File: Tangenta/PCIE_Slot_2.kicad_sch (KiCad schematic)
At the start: 12 parts, among them J19 1-2199230-5

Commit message: Removing component association with previous project (local) libraries.
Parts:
- C112, C113: footprint CholaFootprintsPrjLib:CAP_TANTAL_A -> CAP_TANTAL_A:CAP_TANTAL_A; symbol CholaSymbolsPrjLib:CA45-A-6_3V-47UF-K -> CA45-A-6_3V-47UF-K:CA45-A-6_3V-47UF-K
- H16, H17, H18: symbol CholaSymbolsPrjLib:MountingHole -> MountingHole:MountingHole
- J19: footprint CholaFootprintsPrjLib:M2_Slot -> M2_Slot:M2_Slot; symbol CholaSymbolsPrjLib:1-2199230-5 -> 1-2199230-5:1-2199230-5
- R83, R84, R85, R86, R87: symbol CholaSymbolsPrjLib:R_Small_US -> R_Small_US:R_Small_US
- TP2: symbol CholaSymbolsPrjLib:TestPoint_Small -> TestPoint_Small:TestPoint_Small
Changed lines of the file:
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@@
 	)
 	(symbol
-		(lib_id "CholaSymbolsPrjLib:MountingHole")
+		(lib_id "MountingHole:MountingHole")
 		(at 163.195 175.26 0)
 		(unit 1)
@@
 	)
 	(symbol
-		(lib_id "CholaSymbolsPrjLib:MountingHole")
+		(lib_id "MountingHole:MountingHole")
 		(at 163.195 185.42 0)
 		(unit 1)
@@
 	)
 	(symbol
-		(lib_id "CholaSymbolsPrjLib:R_Small_US")
+		(lib_id "R_Small_US:R_Small_US")
 		(at 161.29 48.26 270)
 		(unit 1)
@@
 	)
 	(symbol
-		(lib_id "CholaSymbolsPrjLib:1-2199230-5")
+		(lib_id "1-2199230-5:1-2199230-5")
 		(at 135.89 33.02 90)
 		(mirror x)
@@
 			)
 		)
-		(property "Footprint" "CholaFootprintsPrjLib:M2_Slot"
+		(property "Footprint" "M2_Slot:M2_Slot"
 			(at 225.73 128.27 0)
 			(effects
@@
 	(symbol
 		(lib_name "CA45-A-6_3V-47UF-K_1")
-		(lib_id "CholaSymbolsPrjLib:CA45-A-6_3V-47UF-K")
+		(lib_id "CA45-A-6_3V-47UF-K:CA45-A-6_3V-47UF-K")
 		(at 140.97 148.59 270)
 		(mirror x)
@@
 			)
 		)
-		(property "Footprint" "CholaFootprintsPrjLib:CAP_TANTAL_A"
+		(property "Footprint" "CAP_TANTAL_A:CAP_TANTAL_A"
 			(at 129.286 145.542 0)
 			(effects
@@
 	)
 	(symbol
-		(lib_id "CholaSymbolsPrjLib:MountingHole")
+		(lib_id "MountingHole:MountingHole")
 		(at 163.195 180.34 0)
 		(unit 1)
@@
 	)
 	(symbol
-		(lib_id "CholaSymbolsPrjLib:R_Small_US")
+		(lib_id "R_Small_US:R_Small_US")
 		(at 161.29 45.72 270)
 		(unit 1)
@@
 	)
 	(symbol
-		(lib_id "CholaSymbolsPrjLib:R_Small_US")
+		(lib_id "R_Small_US:R_Small_US")
 		(at 163.83 91.44 270)
 		(unit 1)
@@
 	)
 	(symbol
-		(lib_id "CholaSymbolsPrjLib:CA45-A-6_3V-47UF-K")
+		(lib_id "CA45-A-6_3V-47UF-K:CA45-A-6_3V-47UF-K")
 		(at 130.175 148.59 270)
 		(mirror x)
@@
 			)
 		)
-		(property "Footprint" "CholaFootprintsPrjLib:CAP_TANTAL_A"
+		(property "Footprint" "CAP_TANTAL_A:CAP_TANTAL_A"
 			(at 118.491 145.542 0)
 			(effects
@@
 	)
 	(symbol
-		(lib_id "CholaSymbolsPrjLib:TestPoint_Small")
+		(lib_id "TestPoint_Small:TestPoint_Small")
 		(at 113.03 114.3 0)
 		(mirror y)
@@
 	)
 	(symbol
-		(lib_id "CholaSymbolsPrjLib:R_Small_US")
+		(lib_id "R_Small_US:R_Small_US")
 		(at 163.83 88.9 270)
 		(unit 1)
@@
 	)
 	(symbol
-		(lib_id "CholaSymbolsPrjLib:R_Small_US")
+		(lib_id "R_Small_US:R_Small_US")
 		(at 34.29 45.72 270)
 		(unit 1)

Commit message: Fixes, before checks.
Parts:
- C112, C113: symbol CA45-A-6_3V-47UF-K:CA45-A-6_3V-47UF-K -> CAP_TANTAL_A:CA45-A-6_3V-47UF-K
- H16, H17, H18: symbol MountingHole:MountingHole -> Mechanical:MountingHole
- J19: symbol 1-2199230-5:1-2199230-5 -> M2_Slot:1-2199230-5
- R83, R84, R85, R86, R87: symbol R_Small_US:R_Small_US -> Device:R_Small_US
- TP2: symbol TestPoint_Small:TestPoint_Small -> Connector:TestPoint_Small
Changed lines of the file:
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@@
 	)
 	(symbol
-		(lib_id "MountingHole:MountingHole")
+		(lib_id "Mechanical:MountingHole")
 		(at 163.195 175.26 0)
 		(unit 1)
@@
 	)
 	(symbol
-		(lib_id "MountingHole:MountingHole")
+		(lib_id "Mechanical:MountingHole")
 		(at 163.195 185.42 0)
 		(unit 1)
@@
 	)
 	(symbol
-		(lib_id "R_Small_US:R_Small_US")
+		(lib_id "Device:R_Small_US")
 		(at 161.29 48.26 270)
 		(unit 1)
@@
 	)
 	(symbol
-		(lib_id "1-2199230-5:1-2199230-5")
+		(lib_id "M2_Slot:1-2199230-5")
 		(at 135.89 33.02 90)
 		(mirror x)
@@
 	(symbol
 		(lib_name "CA45-A-6_3V-47UF-K_1")
-		(lib_id "CA45-A-6_3V-47UF-K:CA45-A-6_3V-47UF-K")
+		(lib_id "CAP_TANTAL_A:CA45-A-6_3V-47UF-K")
 		(at 140.97 148.59 270)
 		(mirror x)
@@
 	)
 	(symbol
-		(lib_id "MountingHole:MountingHole")
+		(lib_id "Mechanical:MountingHole")
 		(at 163.195 180.34 0)
 		(unit 1)
@@
 	)
 	(symbol
-		(lib_id "R_Small_US:R_Small_US")
+		(lib_id "Device:R_Small_US")
 		(at 161.29 45.72 270)
 		(unit 1)
@@
 	)
 	(symbol
-		(lib_id "R_Small_US:R_Small_US")
+		(lib_id "Device:R_Small_US")
 		(at 163.83 91.44 270)
 		(unit 1)
@@
 	)
 	(symbol
-		(lib_id "CA45-A-6_3V-47UF-K:CA45-A-6_3V-47UF-K")
+		(lib_id "CAP_TANTAL_A:CA45-A-6_3V-47UF-K")
 		(at 130.175 148.59 270)
 		(mirror x)
@@
 	)
 	(symbol
-		(lib_id "TestPoint_Small:TestPoint_Small")
+		(lib_id "Connector:TestPoint_Small")
 		(at 113.03 114.3 0)
 		(mirror y)
@@
 	)
 	(symbol
-		(lib_id "R_Small_US:R_Small_US")
+		(lib_id "Device:R_Small_US")
 		(at 163.83 88.9 270)
 		(unit 1)
@@
 	)
 	(symbol
-		(lib_id "R_Small_US:R_Small_US")
+		(lib_id "Device:R_Small_US")
 		(at 34.29 45.72 270)
 		(unit 1)

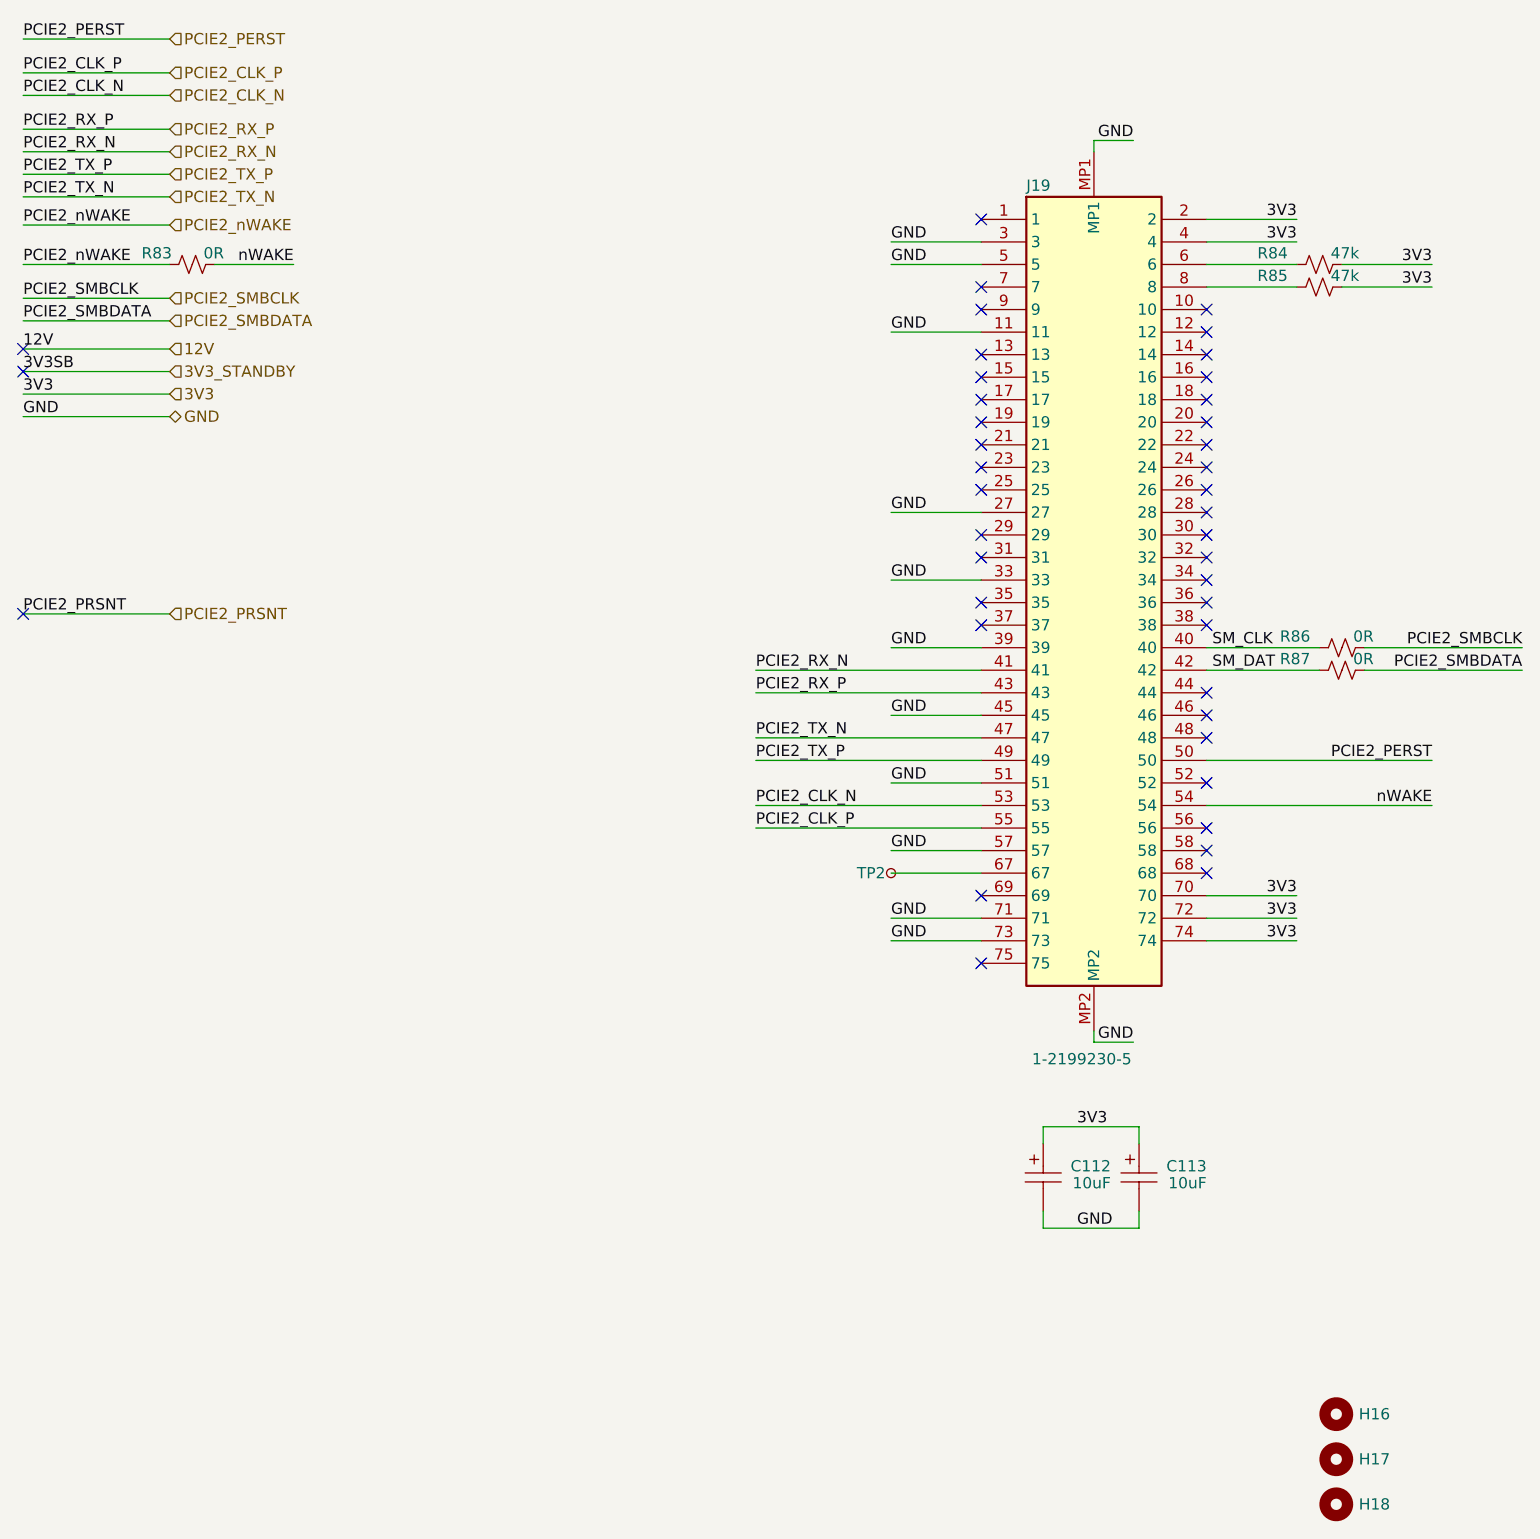
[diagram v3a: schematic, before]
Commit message: Reverting to the original design.
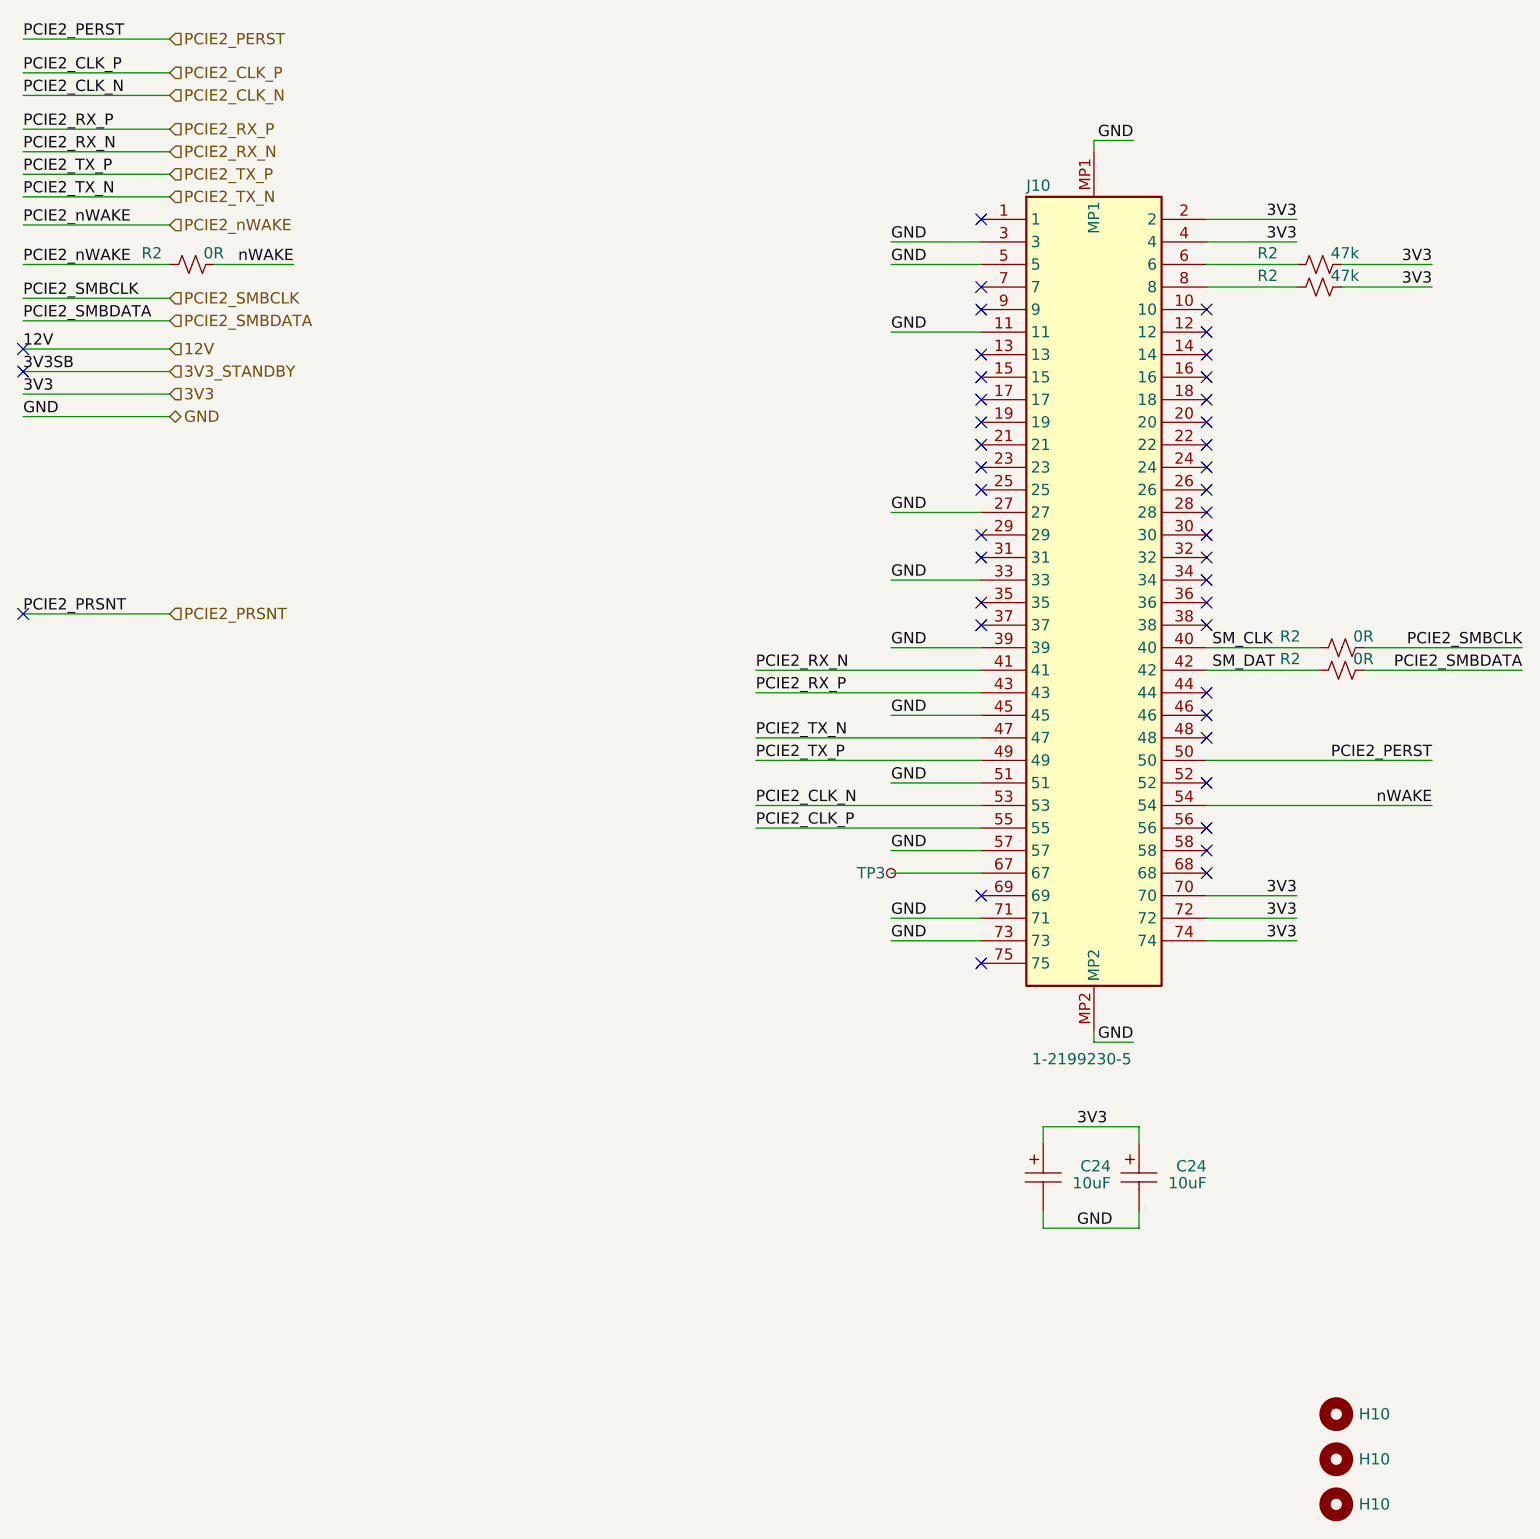
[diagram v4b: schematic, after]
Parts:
- C24: renamed from C113; symbol CAP_TANTAL_A:CA45-A-6_3V-47UF-K -> CholaSymbolsPrjLib:CA45-A-6_3V-47UF-K; Capacitance 47uF -> 10uF; LCSC C129570 -> C119051
- C24: renamed from C112; symbol CAP_TANTAL_A:CA45-A-6_3V-47UF-K -> CholaSymbolsPrjLib:CA45-A-6_3V-47UF-K; Capacitance 47uF -> 10uF; LCSC C129570 -> C119051
- H10: renamed from H16; symbol Mechanical:MountingHole -> CholaSymbolsPrjLib:MountingHole
- H10: renamed from H18; symbol Mechanical:MountingHole -> CholaSymbolsPrjLib:MountingHole
- H10: renamed from H17; symbol Mechanical:MountingHole -> CholaSymbolsPrjLib:MountingHole
- J10: renamed from J19; symbol M2_Slot:1-2199230-5 -> CholaSymbolsPrjLib:1-2199230-5
- R2: renamed from R85; symbol Device:R_Small_US -> CholaSymbolsPrjLib:R_Small_US
- R2: renamed from R84; symbol Device:R_Small_US -> CholaSymbolsPrjLib:R_Small_US
- R2: renamed from R87; symbol Device:R_Small_US -> CholaSymbolsPrjLib:R_Small_US
- R2: renamed from R86; symbol Device:R_Small_US -> CholaSymbolsPrjLib:R_Small_US
- R2: renamed from R83; symbol Device:R_Small_US -> CholaSymbolsPrjLib:R_Small_US
- TP3: renamed from TP2; symbol Connector:TestPoint_Small -> CholaSymbolsPrjLib:TestPoint_Small

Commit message: initialize branch
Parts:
- renumbered C24 to C112, C24 to C113, H10 to H16, H10 to H17, H10 to H18, J10 to J19, R2 to R83, R2 to R84, R2 to R85, R2 to R86, R2 to R87, TP3 to TP2

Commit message: M2_Slot, PCIE_x16_Slot, PCIE_Switch
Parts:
- J19: footprint M2_Slot:M2_Slot -> CholaFootprintsPrjLib:M2_Slot
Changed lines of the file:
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@@
       (effects (font (size 1.27 1.27)) (justify right))
     )
-    (property "Footprint" "M2_Slot:M2_Slot" (at 225.73 128.27 0)
+    (property "Footprint" "CholaFootprintsPrjLib:M2_Slot" (at 225.73 128.27 0)
       (effects (font (size 1.27 1.27)) (justify left top) hide)
     )

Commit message: CAP_L6, CAP_TANTAL_A, M24C04-RMN6TP
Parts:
- C112, C113: footprint CAP_TANTAL_A:CAP_TANTAL_A -> CholaFootprintsPrjLib:CAP_TANTAL_A; Capacitance 10uF -> 47uF; LCSC C119051 -> C129570
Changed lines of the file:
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@@
     )
   )
-  (symbol (lib_id "CholaSymbolsPrjLib:CA45-A-6_3V-47UF-K") (at 140.97 148.59 270) (mirror x) (unit 1)
+  (symbol (lib_name "CA45-A-6_3V-47UF-K_1") (lib_id "CholaSymbolsPrjLib:CA45-A-6_3V-47UF-K") (at 140.97 148.59 270) (mirror x) (unit 1)
     (in_bom yes) (on_board yes) (dnp no)
     (property "Reference" "C113" (at 148.59 147.32 90)
@@
       (effects (font (size 1.27 1.27)) (justify right))
     )
-    (property "Footprint" "CAP_TANTAL_A:CAP_TANTAL_A" (at 129.286 145.542 0)
+    (property "Footprint" "CholaFootprintsPrjLib:CAP_TANTAL_A" (at 129.286 145.542 0)
       (effects (font (size 1.27 1.27) italic) hide)
     )
-    (property "Datasheet" "" (at 127 158.75 0)
+    (property "Datasheet" "https://item.szlcsc.com/2057730.html" (at 127 158.75 0)
       (effects (font (size 1.27 1.27)) (justify left) hide)
     )
-    (property "LCSC" "C119051" (at 133.858 154.686 0)
+    (property "LCSC" "C129570" (at 133.858 154.686 0)
       (effects (font (size 1.27 1.27)) hide)
     )
-    (property "Capacitance" "10uF" (at 137.668 148.336 0)
+    (property "Capacitance" "47uF" (at 137.668 148.336 0)
       (effects (font (size 1.27 1.27)) hide)
     )
@@
       (effects (font (size 1.27 1.27)) (justify right))
     )
-    (property "Footprint" "CAP_TANTAL_A:CAP_TANTAL_A" (at 118.491 145.542 0)
+    (property "Footprint" "CholaFootprintsPrjLib:CAP_TANTAL_A" (at 118.491 145.542 0)
       (effects (font (size 1.27 1.27) italic) hide)
     )
-    (property "Datasheet" "" (at 116.205 158.75 0)
+    (property "Datasheet" "https://item.szlcsc.com/2057730.html" (at 116.205 158.75 0)
       (effects (font (size 1.27 1.27)) (justify left) hide)
     )
-    (property "LCSC" "C119051" (at 123.063 154.686 0)
+    (property "LCSC" "C129570" (at 123.063 154.686 0)
       (effects (font (size 1.27 1.27)) hide)
     )
-    (property "Capacitance" "10uF" (at 126.873 148.336 0)
+    (property "Capacitance" "47uF" (at 126.873 148.336 0)
       (effects (font (size 1.27 1.27)) hide)
     )
